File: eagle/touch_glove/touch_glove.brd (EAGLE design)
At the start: 160 x 100 mm, 35 parts, among them U1 DRV8830

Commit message: Added Peltier driving circuitry
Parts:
- added C10, C13, C16, C19, C22: CAP_POL_ALUM-ELECTROLYTIC_SMD_100UF-16V-20%, MrSwirlyEyes:CAP_POL_ALUM-ELECTROLYTIC_100UF-16V-20%_6.3LW-6.10H
- added C11, C12, C14, C15, C17, C18, C20, C21, C8, C9: CAP_CER_SMD-805_0.1UF-50V-10%, MrSwirlyEyes:CAP_CER_SMD-805_0.1UF-50V-10%
- added P1, P2, P3, P4, P5: PELTIER-CM23-1.9-05AC_1.9A-2.8V_8X6X2MM, MrSwirlyEyes:CONNECTOR_PELTIER
- added U2, U3, U4, U5, U6: DRV8837C_H-BRIDGE_1A_WSON-8-PAD, MrSwirlyEyes:WSON-8-PAD
- VIBE_1, VIBE_2, VIBE_3, VIBE_4, VIBE_5: device MrSwirlyEyes:CONNECTOR-01X02 -> MrSwirlyEyes:CONNECTOR_VIBE-MOTOR
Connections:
- new net N$1: P2.HOT, U3.2
- new net N$11: P3.HOT, U4.2
- new net N$12: P3.COLD, U4.3
- new net N$13: P1.HOT, U2.2
- new net N$14: P1.COLD, U2.3
- new net N$16: P4.HOT, U5.2
- new net N$18: P4.COLD, U5.3
- new net N$19: P5.HOT, U6.2
- new net N$20: P5.COLD, U6.3
- new net N$5: P2.COLD, U3.3
- net GND: now also C10.K, C11.2, C12.2, C13.K, C14.2, C15.2, C16.K, C17.2, C18.2, C19.K, C20.2, C21.2, C22.K, C8.2, C9.2, U2.4, U2.GND, U3.4, U3.GND, U4.4, U4.GND, U5.4, U5.GND, U6.4, U6.GND
- net TEC_1_COLD: now also U2.5
- net TEC_1_HOT: now also U2.6
- net TEC_2_COLD: now also U3.5
- net TEC_2_HOT: now also U3.6
- net TEC_3_COLD: now also U4.5
- net TEC_3_HOT: now also U4.6
- net TEC_4_COLD: now also U5.5
- net TEC_4_HOT: now also U5.6
- net TEC_5_COLD: now also U6.5
- net TEC_5_HOT: now also U6.6
- net VCC: now also C10.A, C11.1, C12.1, C13.A, C14.1, C15.1, C16.A, C17.1, C18.1, C19.A, C20.1, C21.1, C22.A, C8.1, C9.1, U2.1, U2.7, U2.8, U3.1, U3.7, U3.8, U4.1, U4.7, U4.8, U5.1, U5.7, U5.8, U6.1, U6.7, U6.8

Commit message: Modfied git ignore.  Added h bridge files.  Modified EAGLE files
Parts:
- removed U1: DRV8830, SparkFun-Retired:MSOP-10-GNDPAD
- added F1: FSR, MrSwirlyEyes:CONNECTOR_FSR
- added R11: 10KΩ, MrSwirlyEyes:RESC2012X60_HS
- C1, C11, C12, C14, C15, C17, C18, C20, C21, C3, C4, C5, C6, C7, C8, C9: value CAP_CER_SMD-805_0.1UF-50V-10% -> 0.1uF/50V; device MrSwirlyEyes:CAP_CER_SMD-805_0.1UF-50V-10% -> MrSwirlyEyes:CAP_CER_SMD-805
- C10, C13, C16, C19, C22: value CAP_POL_ALUM-ELECTROLYTIC_SMD_100UF-16V-20% -> 100UF/16V; device MrSwirlyEyes:CAP_POL_ALUM-ELECTROLYTIC_100UF-16V-20%_6.3LW-6.10H -> MrSwirlyEyes:CAP_POL_ALUM-ELECTROLYTIC
- C2: value CAP_CER_SMD-805_10UF-25V-10% -> 10uF/25V; device MrSwirlyEyes:CAP_CER_SMD-805_10UF-25V-10% -> MrSwirlyEyes:CAP_CER_SMD-805
- D1, D2, D3, D4, D5: value DIODE_SMD_GP_1A-50V-SOD123F -> 1A/50V
- DEMUX: value CD74HC4067-SM96_16:1_MUX-DEMUX -> CH16_MUX-DEMUX; device MrSwirlyEyes:SSOP24 -> MrSwirlyEyes:SSOP-24
- P1, P2, P3, P4, P5: value PELTIER-CM23-1.9-05AC_1.9A-2.8V_8X6X2MM -> PELTIER
- PWM_DRIVER: value PCA9685_16-CH_12-BIT_PWM-DRIVER -> PCA9685; device MrSwirlyEyes:TSSOP28 -> MrSwirlyEyes:TSSOP-28
- R1, R10, R2, R3, R4, R5, R6, R7, R8, R9: value RES_SMD-805_10K-5%-1/8W -> 10KΩ; device MrSwirlyEyes:RES_SMD-805_10K-5%-1/8W -> MrSwirlyEyes:RESC2012X60_HS
- U2, U3, U4, U5, U6: value DRV8837C_H-BRIDGE_1A_WSON-8-PAD -> DRV8837C; device MrSwirlyEyes:WSON-8-PAD -> MrSwirlyEyes:WSON-8-PPAD
- VIBE_T1, VIBE_T2, VIBE_T3, VIBE_T4, VIBE_T5: value SI2302CDS-MOSFET-N-CH_2.6A_20V_57MΩ_SOT23-3 -> 2.6A/20V/57mΩ
- moved U4 10.9 mm to (-35.6, -435.6)
- moved C16 6.35 mm to (-33.0, -428.0)
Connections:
- removed net C15: DEMUX.16
- removed net OUT1: U1.3
- removed net OUT2: U1.1
- removed net PPAD: U1.GND
- new net FSR_1: DEMUX.16, F1.-, R11.2
- net GND: now also R11.1; no longer U1.5
- net VCC: now also F1.+; no longer U1.4

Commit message: Modified gitignore.  Tons of progress on PCB for Touch Glove
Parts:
- removed F1: FSR, MrSwirlyEyes:CONNECTOR_FSR
- added A1: ANTENNASMD5, lib_kenmei:ANTENNA-CHIP5
- added B1: 748421245, lib_kenmei:0805_BALUN
- added C23, C27, C28, C29: 10uF/25V, MrSwirlyEyes:CAP_CER_SMD-805
- added C24, C25, C26, C30, C31, C32, C33, C34, C35, C37, C39, C46: 0.1uF/50V, MrSwirlyEyes:CAP_CER_SMD-805
- added C36, C38, C40, C41, C47: 1uF/25V, MrSwirlyEyes:CAP_CER_SMD-805
- added C42, C43: 12pF/250V, MrSwirlyEyes:CAP_CER_SMD-805
- added C44: 22PF/250V, MrSwirlyEyes:CAP_CER_SMD-805
- added C45: 0.75PF/100V, MrSwirlyEyes:CAP_CER_SMD-805
- added FLEX1, FLEX2, FLEX3, FLEX4, FLEX5: 10K, MrSwirlyEyes:CONNECTOR_FSR
- added R12, R13: 4.7K, MrSwirlyEyes:RESC2012X60_HS
- added R14, R16, R18, R20, R22, R24, R26, R28, R30, R32, R34, R35, R36, R37, R38: 10KΩ, MrSwirlyEyes:RESC2012X60_HS
- added R15, R17, R19, R21, R23, R25, R27, R29, R31, R33: 100Ω, MrSwirlyEyes:RESC2012X60_HS
- added U1: DRV8837C, MrSwirlyEyes:WSON-8-PPAD
- added Y1: 16MHz, MrSwirlyEyes:CRYSTAL-SMD-5X3
- C1, C11, C14, C15, C18: value 0.1uF/50V -> 10uF/25V
- C10, C19, C22: value 100UF/16V -> 10uF/25V; device MrSwirlyEyes:CAP_POL_ALUM-ELECTROLYTIC -> MrSwirlyEyes:CAP_CER_SMD-805
- C13, C16: value 100UF/16V -> 0.1uF/50V; device MrSwirlyEyes:CAP_POL_ALUM-ELECTROLYTIC -> MrSwirlyEyes:CAP_CER_SMD-805
- C2: value 10uF/25V -> 0.1uF/50V
- R10, R6, R7, R8, R9: value 10KΩ -> 100Ω
- U6: value DRV8837C -> ATMEGA128RFA1; device MrSwirlyEyes:WSON-8-PPAD -> MrSwirlyEyes:VFQFN-64
- moved U6 425.1 mm to (-92.7, -915.7)
- moved P1 416.5 mm to (-87.6, -675.6)
- moved U2 376.7 mm to (-95.2, -720.1)
- moved U3 364.2 mm to (-95.2, -750.6)
- moved C8 339.8 mm to (-90.2, -689.6)
- moved C9 334.0 mm to (-83.8, -689.6)
- moved P2 331.6 mm to (-87.6, -706.1)
- moved C13 329.4 mm to (-83.8, -720.1)
- moved P3 327.8 mm to (-87.6, -736.6)
- moved C16 327.6 mm to (-90.2, -750.6)
- moved U5 326.8 mm to (-95.2, -781.0)
- moved C10 326.2 mm to (-78.7, -689.6)
- moved C12 323.4 mm to (-90.2, -720.1)
- moved C19 298.6 mm to (-95.2, -755.6)
- moved C11 298.0 mm to (-95.2, -694.7)
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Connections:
- new net A0: U6.63
- new net A1: U6.64
- new net A2: U6.1
- new net A3: U6.2
- new net A4: U6.3
- new net A5: U6.4
- new net A6: U6.5
- new net A7: U6.6
- new net C15: DEMUX.16
- new net FSR_2: FLEX2.-, R34.2
- new net FSR_3: FLEX3.-, R35.2
- new net FSR_4: FLEX4.-, R36.2
- new net FSR_5: FLEX5.-, R37.2
- new net MISO: U6.39
- new net MOSI: U6.38
- new net N$21: R9.2, VIBE_T4.G
- new net N$22: R10.2, VIBE_T5.G
- new net N$23: P5.HOT, U5.2
- new net N$24: P5.COLD, U5.3
- new net N$25: R27.2, U5.5
- new net N$26: R29.2, U5.6
- new net N$27: P4.HOT, U4.2
- new net N$28: P4.COLD, U4.3
- new net N$29: R31.2, U4.5
- new net N$30: C43.1, U6.57, Y1.3
- new net N$31: R33.2, U4.6
- new net N$32: B1.3, U6.9
- new net N$33: B1.4, U6.8
- new net N$34: B1.2, C44.1
- new net N$35: C42.1, U6.56, Y1.1
- new net N$39: A1.FEED, B1.1, C45.1
- new net PB4: U6.40
- new net PB5: U6.41
- new net PB6: U6.42
- new net PB7: U6.43
- new net PD4: U6.29
- new net PD5: U6.30
- new net PD6: U6.31
- new net PD7: U6.32
- new net PE2: U6.48
- new net PE3: U6.49
- new net PE4: U6.50
- new net PE5: U6.51
- new net PE6: U6.52
- new net PE7: U6.53
- new net PG0: U6.14
- new net PG1: U6.15
- new net PG2: U6.16
- new net PG3: U6.17
- new net PG4: U6.18
- new net PG5: U6.19
- new net RESET: R38.1, U6.12
- new net RX0: U6.46
- new net RX1: U6.27
- new net SCK: U6.37
- new net SS: U6.36
- new net TX0: U6.47
- new net TX1: U6.28
- new net VM: C10.1, C13.1, C14.1, C17.1, C18.1, C21.1, C22.1, C26.1, C27.1, C9.1, U1.1, U2.1, U3.1, U4.1, U5.1
- net FSR_1: now also FLEX1.-; no longer DEMUX.16, F1.-
- net GND: now also B1.5, C10.2, C13.2, C16.2, C19.2, C22.2, C23.2, C24.2, C25.2, C26.2, C27.2, C28.2, C29.2, C30.2, C31.2, C32.2, C33.2, C34.2, C35.2, C36.2, C37.2, C38.2, C39.2, C40.2, C41.2, C42.2, C43.2, C44.2, C45.2, C46.2, C47.2, R14.1, R16.1, R18.1, R20.1, R22.1, R24.1, R26.1, R28.1, R30.1, R32.1, R34.1, R35.1, R36.1, R37.1, U1.4, U1.GND, U6.10, U6.11, U6.20, U6.24, U6.33, U6.35, U6.45, U6.55, U6.58, U6.61, U6.7; no longer C10.K, C13.K, C16.K, C19.K, C22.K, U6.4, U6.GND
- net N$1: now also P1.HOT, U1.2; no longer P2.HOT, U3.2
- net N$10: now also R17.2, U1.6; no longer R7.1
- net N$11: now also P2.HOT, U2.2; no longer P3.HOT, U4.2
- net N$12: now also P2.COLD, U2.3; no longer P3.COLD, U4.3
- net N$13: now also R19.2, U2.5; no longer P1.HOT, U2.2
- net N$14: now also R21.2, U2.6; no longer P1.COLD, U2.3
- net N$16: now also P3.HOT, U3.2; no longer P4.HOT, U5.2
- net N$18: now also P3.COLD, U3.3; no longer P4.COLD, U5.3
- net N$19: now also R23.2, U3.5; no longer P5.HOT, U6.2
- net N$20: now also R25.2, U3.6; no longer P5.COLD, U6.3
- net N$5: now also P1.COLD, U1.3; no longer P2.COLD, U3.3
- net N$6: now also R6.2, VIBE_T1.G; no longer R6.1
- net N$7: now also R7.2, VIBE_T2.G; no longer R10.1
- net N$8: now also R15.2, U1.5; no longer R9.1
- net N$9: now also R8.2, VIBE_T3.G; no longer R8.1
- net SCL: now also R13.1, U6.25
- net SDA: now also R12.1, U6.26
- net TEC_1_COLD: now also R26.2, R27.1; no longer U2.5
- net TEC_1_HOT: now also R28.2, R29.1; no longer U2.6
- net TEC_2_COLD: now also R22.2, R23.1; no longer U3.5
- net TEC_2_HOT: now also R24.2, R25.1; no longer U3.6
- net TEC_3_COLD: now also R18.2, R19.1; no longer U4.5
- net TEC_3_HOT: now also R20.2, R21.1; no longer U4.6
- net TEC_4_COLD: now also R14.2, R15.1; no longer U5.5
- net TEC_4_HOT: now also R16.2, R17.1; no longer U5.6
- net TEC_5_COLD: now also R30.2, R31.1; no longer U6.5
- net TEC_5_HOT: now also R32.2, R33.1; no longer U6.6
- net VCC: now also C16.1, C19.1, C23.1, C24.1, C25.1, C28.1, C29.1, C30.1, C31.1, C32.1, C33.1, C34.1, C35.1, C36.1, C37.1, C38.1, C39.1, C40.1, C41.1, C46.1, C47.1, FLEX1.+, FLEX2.+, FLEX3.+, FLEX4.+, FLEX5.+, R12.2, R13.2, R38.2, U1.7, U1.8, U6.21, U6.22, U6.23, U6.34, U6.44, U6.54, U6.59, U6.60, U6.62; no longer C10.A, C13.A, C14.1, C16.A, C17.1, C18.1, C19.A, C21.1, C22.A, C9.1, F1.+, U2.1, U3.1, U4.1, U5.1, U6.1, U6.7, U6.8
- net VIBE_1: now also R6.1; no longer R6.2, VIBE_T1.G
- net VIBE_2: now also R7.1; no longer R7.2, VIBE_T2.G
- net VIBE_3: now also R8.1; no longer R8.2, VIBE_T3.G
- net VIBE_4: now also R9.1; no longer R9.2, VIBE_T4.G
- net VIBE_5: now also R10.1; no longer R10.2, VIBE_T5.G

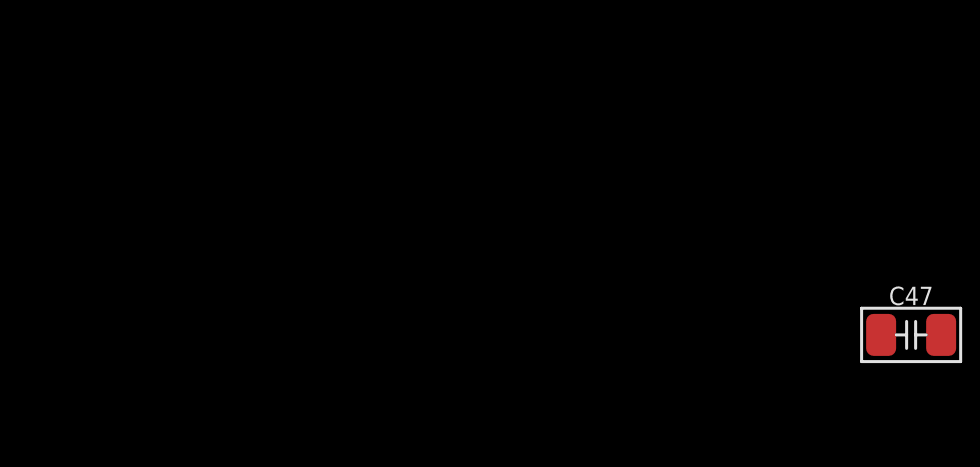
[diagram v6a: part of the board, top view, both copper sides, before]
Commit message: Modified TMP36 temperature sensor library to work with DEMUX.  Added ATMEGA128RFA1 and LM9DS1 IMU to Touch Glove schematic
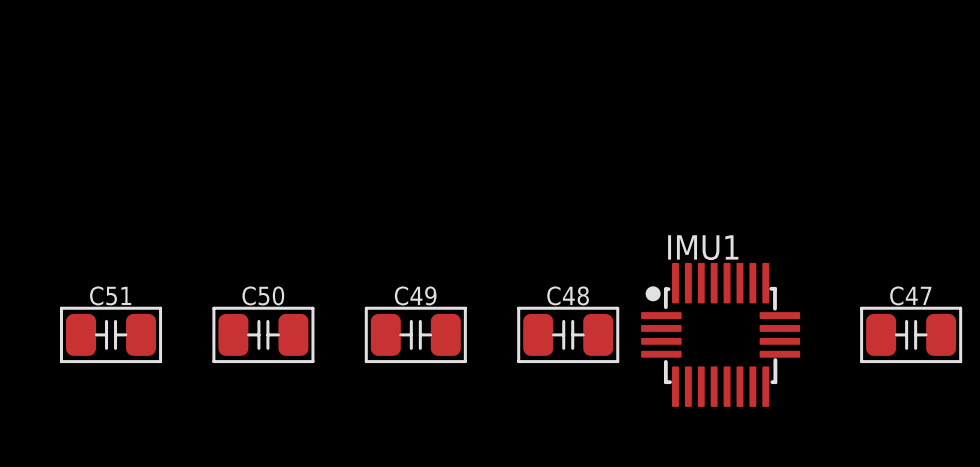
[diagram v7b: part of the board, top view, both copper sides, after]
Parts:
- added C48: 0.22uF/50V, MrSwirlyEyes:CAP_CER_SMD-805
- added C49, C50: 10uF/25V, MrSwirlyEyes:CAP_CER_SMD-805
- added C51: 0.1uF/50V, MrSwirlyEyes:CAP_CER_SMD-805
- added IMU1: LM9DS1, lib_kenmei:LSM9DS1_LGA24L
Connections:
- new net N$36: C49.1, IMU1.21
- new net N$37: C48.1, IMU1.24
- net GND: now also C48.2, C49.2, C50.2, C51.2, IMU1.14, IMU1.15, IMU1.16, IMU1.17, IMU1.18, IMU1.19, IMU1.20
- net SCL: now also IMU1.2, R12.1; no longer R13.1
- net SDA: now also IMU1.4, R13.1; no longer R12.1
- net VCC: now also C50.1, C51.1, IMU1.1, IMU1.22, IMU1.23, IMU1.3

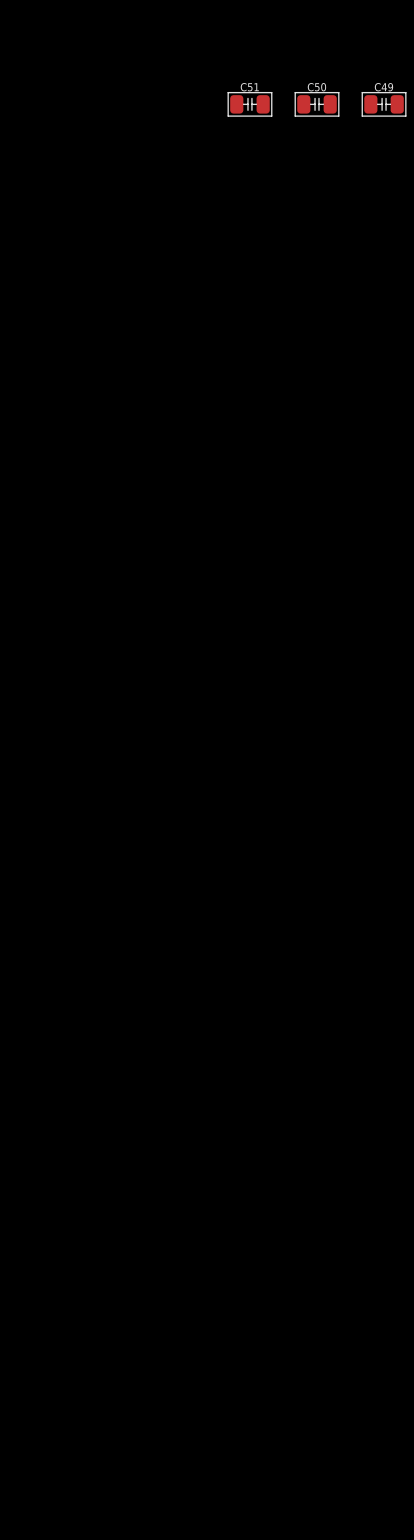
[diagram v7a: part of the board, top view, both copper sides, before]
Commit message: Added FTDI programmer and AVR SPI bootloader pins to schematic
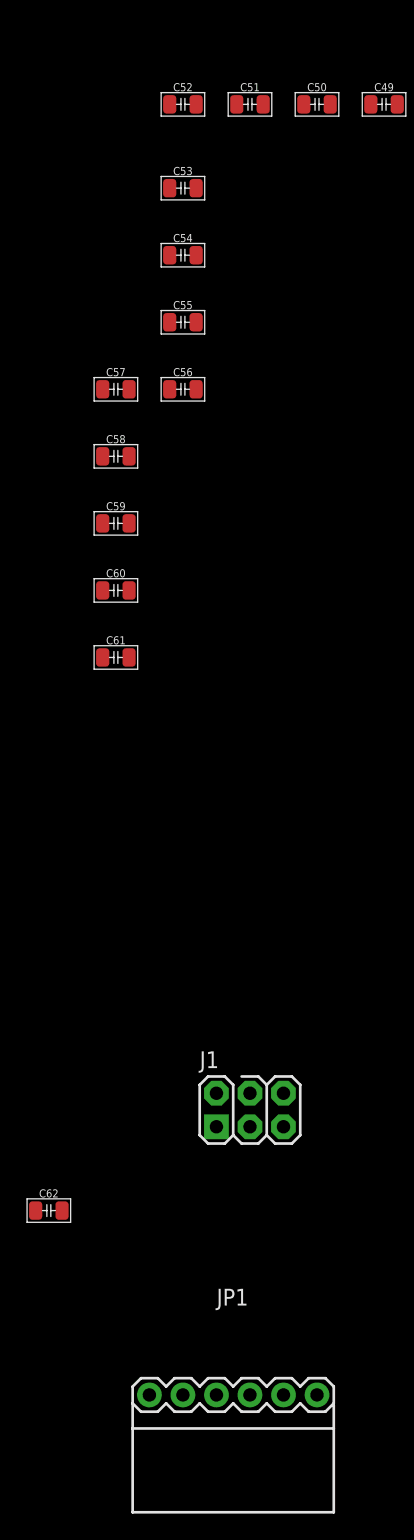
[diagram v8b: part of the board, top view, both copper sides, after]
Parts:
- added C52, C53, C54, C55, C56, C62: 0.1uF/50V, MrSwirlyEyes:CAP_CER_SMD-805
- added C57, C58, C59, C60, C61: 10uF/25V, MrSwirlyEyes:CAP_CER_SMD-805
- added J1: (no value), MrSwirlyEyes:2X3-NS
- added JP1: FTDIPTH-RA, MrSwirlyEyes:FTDI_BASIC-6PIN-MALE-RA
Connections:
- net SS renamed SSN
- new net N$41: C62.1, JP1.DTR
- new net N$42: JP1.CTS
- net GND: now also C52.2, C53.2, C54.2, C55.2, C56.2, C57.2, C58.2, C59.2, C60.2, C61.2, J1.6, JP1.GND
- net MISO: now also J1.1
- net MOSI: now also J1.4
- net RESET: now also C62.2, J1.5
- net RX0: now also JP1.TXO
- net SCK: now also J1.3
- net TX0: now also JP1.RXI
- net VCC: now also C52.1, C53.1, C54.1, C55.1, C56.1, C57.1, C58.1, C59.1, C60.1, C61.1, J1.2, JP1.VCC
